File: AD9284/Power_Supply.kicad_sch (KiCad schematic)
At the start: 22 parts, among them U4 TLV70018DCKR, U5 TLV70018DCKR

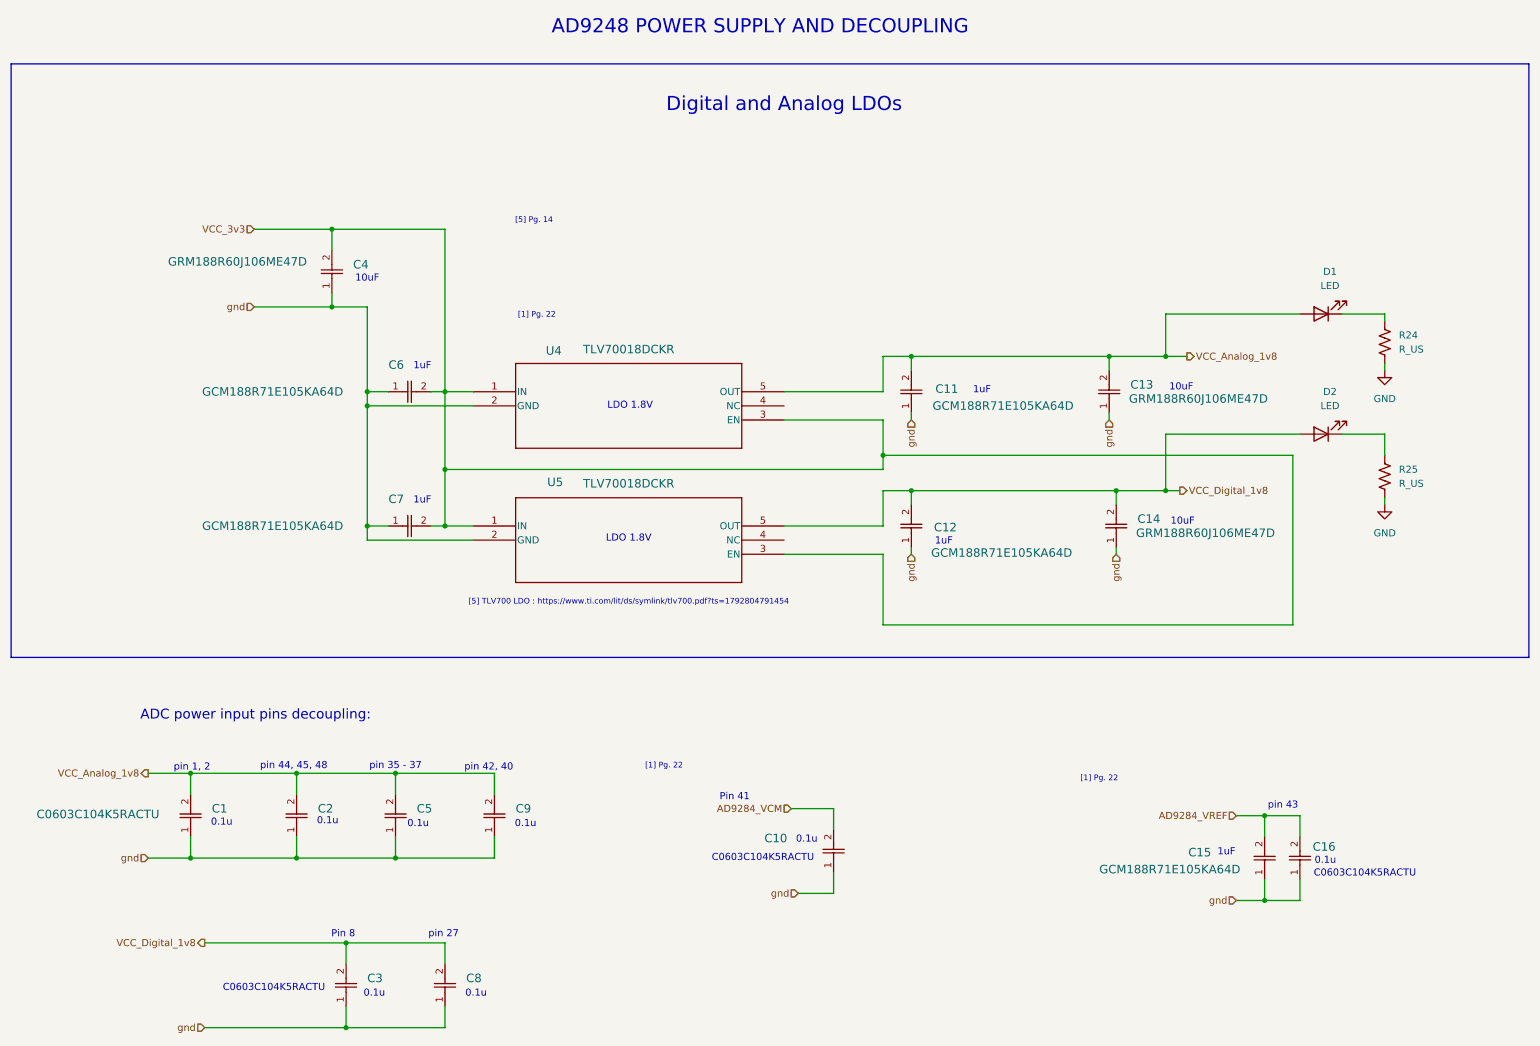
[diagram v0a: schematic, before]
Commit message: Schematic and PCB complete. TODO: BOM
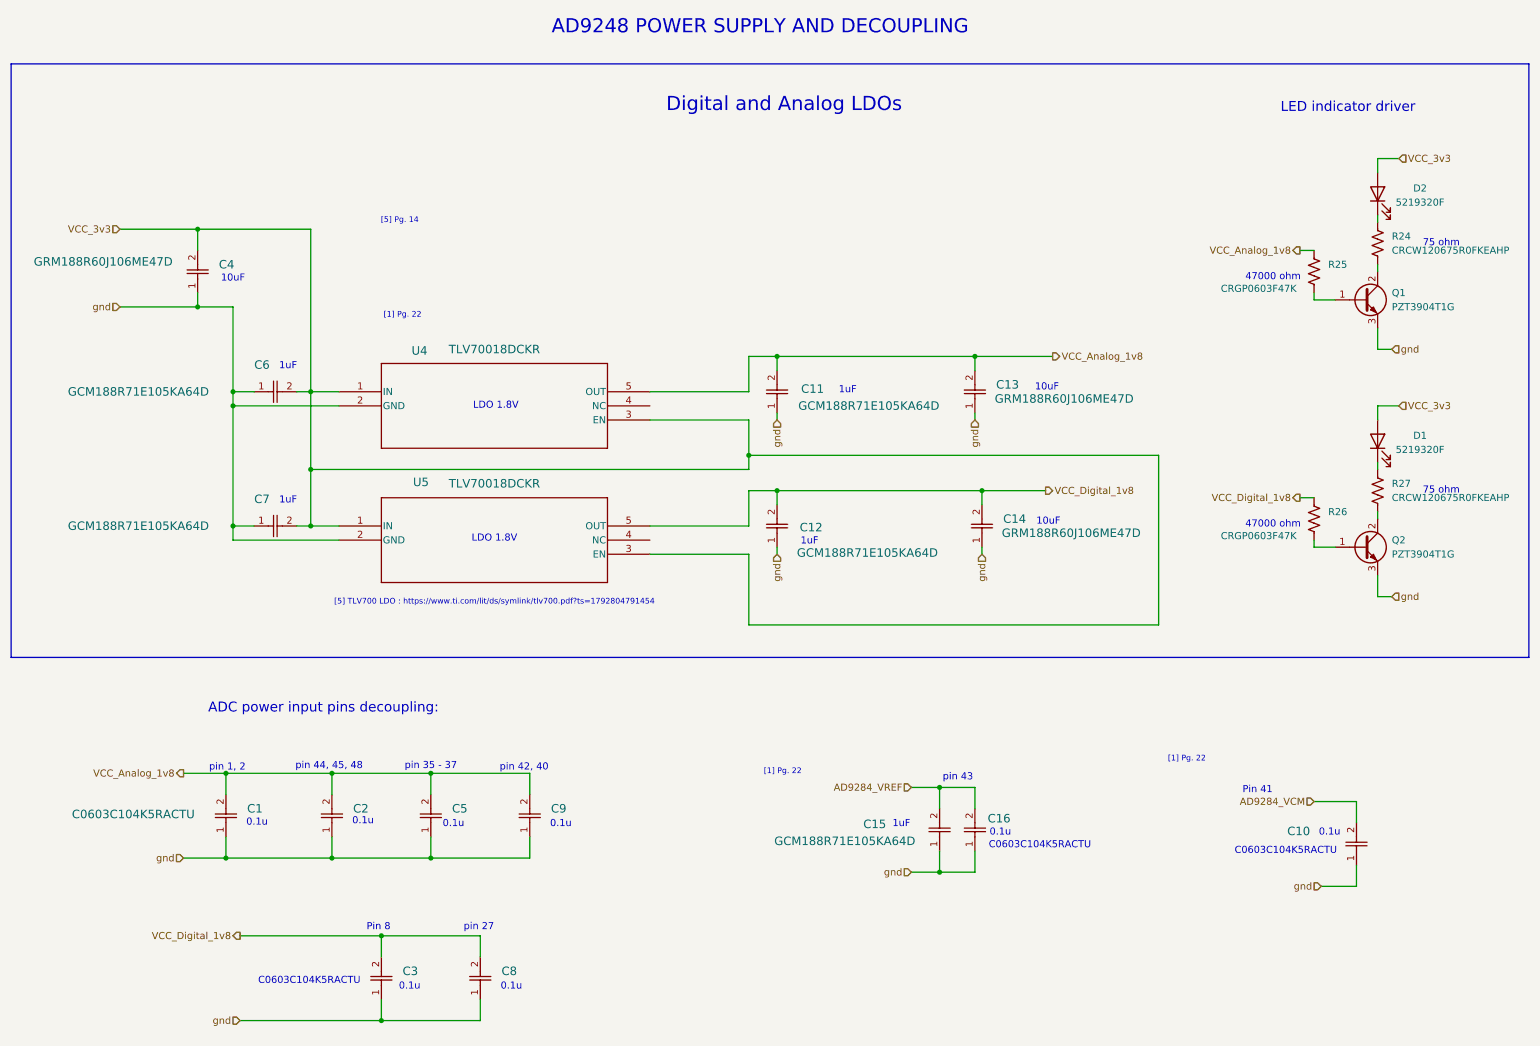
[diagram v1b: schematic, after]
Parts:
- added Q1, Q2: PZT3904T1G, Package_TO_SOT_SMD:SOT-223-3_TabPin2, symbol Transistor_BJT:Q_NPN_BCE
- added R26: CRGP0603F47K, Resistor_SMD:R_0201_0603Metric, symbol Device:R_US
- added R27: CRCW120675R0FKEAHP, Resistor_SMD:R_1206_3216Metric, symbol Device:R_US
- D1, D2: value LED -> 5219320F
- R24: value R_US -> CRCW120675R0FKEAHP; footprint part_library:RC1206FR_0733RL -> Resistor_SMD:R_1206_3216Metric
- R25: value R_US -> CRGP0603F47K; footprint part_library:RC1206FR_0733RL -> Resistor_SMD:R_0201_0603Metric
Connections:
- net VCC_3v3: now also D1.2 (A), D2.2 (A)
- net VCC_Analog_1v8: now also R25.2; no longer D1.2 (A)
- net VCC_Digital_1v8: now also R26.2; no longer D2.2 (A)
- net gnd: now also Q1.3 (E), Q2.3 (E)
- net at R25.1: now also Q1.1 (B); no longer D2.1 (K)
- net at R24.1: now also Q1.2 (C); no longer D1.1 (K)
- net GND: no longer names the net of R24.2
- net GND: now also D2.1 (K); no longer R25.2
- new net: Q2.1 (B), R26.1
- new net: Q2.2 (C), R27.1
- new net: D1.1 (K), R27.2
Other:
- note added: "47000 ohm"
- note added: "75 ohm"
- note added: "LED indicator driver"
- moved on the sheet: C1, C10, C11, C12, C13, C14, C15, C16, C2, C3, C4, C5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
